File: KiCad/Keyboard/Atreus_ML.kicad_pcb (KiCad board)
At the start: 2 copper layers, 86 parts, among them K1 CHERRY_ML, K10 CHERRY_ML, K11 CHERRY_ML, K12 CHERRY_ML, K13 CHERRY_ML, K14 CHERRY_ML, K15 CHERRY_ML, K16 CHERRY_ML, K17 CHERRY_ML, K18 CHERRY_ML, K19 CHERRY_ML, K2 CHERRY_ML, K20 CHERRY_ML, K21 CHERRY_ML, K22 CHERRY_ML, K23 CHERRY_ML, K24 CHERRY_ML, K25 CHERRY_ML, K26 CHERRY_ML, K27 CHERRY_ML, K28 CHERRY_ML, K29 CHERRY_ML, K3 CHERRY_ML, K30 CHERRY_ML, K31 CHERRY_ML, K32 CHERRY_ML, K33 CHERRY_ML, K34 CHERRY_ML, K35 CHERRY_ML, K36 CHERRY_ML, K37 CHERRY_ML, K38 CHERRY_ML, K39 CHERRY_ML, K4 CHERRY_ML, K40 CHERRY_ML, K41 CHERRY_ML, K42 CHERRY_ML, K5 CHERRY_ML, K6 CHERRY_ML, K7 CHERRY_ML, K8 CHERRY_ML, K9 CHERRY_ML, P1 CONN_01X07, U1 TEENSY2.0

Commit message: Switching to teensu compact
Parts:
- moved P1 67.9 mm to (158.0, 104.0), turned to 180 degrees
- moved U1 45.8 mm to (150.0, 80.0)
- moved K2 26.5 mm to (51.0, 86.0)
- moved D2 26.3 mm to (50.0, 97.0)
- moved D6 25.1 mm to (70.0, 96.0)
- moved K6 23.9 mm to (71.0, 86.0)
- moved D1 23.0 mm to (50.0, 76.0)
- moved D5 22.6 mm to (70.0, 73.0)
- moved K1 22.1 mm to (50.0, 67.0)
- moved D10 22.1 mm to (90.0, 91.0)
- moved K5 21.0 mm to (70.0, 64.0)
- moved K10 19.7 mm to (91.0, 81.0)
- moved D9 19.2 mm to (90.0, 68.0)
- moved K9 16.8 mm to (90.0, 59.0)
- moved K35 16.6 mm to (261.0, 56.0)
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
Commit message: Basic Layout done
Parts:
- removed P1: CONN_01X07, Socket_Strips:Socket_Strip_Straight_1x07
- U1: value TEENSY2.0 -> TEENSY2.0-Compact; footprint Teensy:TEENSY_2.0 -> Teensy:TEENSY_2.0-Compact
- moved D12 44.3 mm to (90.0, 128.0)
- moved D4 42.6 mm to (50.0, 136.0)
- moved D8 41.5 mm to (70.0, 133.0)
- moved U1 41.4 mm to (156.0, 39.0)
- moved K4 39.9 mm to (50.0, 127.0)
- moved D3 39.8 mm to (50.0, 116.0)
- moved D7 38.8 mm to (70.0, 113.0)
- moved K12 38.5 mm to (90.0, 119.0)
- moved K8 38.3 mm to (70.0, 124.0)
- moved K3 35.4 mm to (50.0, 107.0)
- moved D16 34.8 mm to (110.0, 134.0)
- moved K7 33.7 mm to (70.0, 104.0)
- moved D11 32.9 mm to (90.0, 108.0)
- moved K11 30.7 mm to (90.0, 99.0)
- moved D34 29.6 mm to (230.0, 128.0), turned to 0 degrees
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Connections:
- U1 pad 19: Net-(K21-Pad4) -> Net-(U1-Pad19)

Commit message: Rotation done
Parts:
- moved D20 25.2 mm to (105.3, 145.3), turned to 350 degrees
- moved D21 24.9 mm to (126.8, 138.9), turned to 170 degrees
- moved D4 24.3 mm to (27.2, 127.5), turned to 350 degrees
- moved K20 23.6 mm to (107.1, 135.5), turned to 350 degrees
- moved D16 23.4 mm to (86.7, 135.9), turned to 350 degrees
- moved K21 23.3 mm to (128.5, 129.1), turned to 350 degrees
- moved D8 23.1 mm to (47.5, 128.0), turned to 350 degrees
- moved K4 22.8 mm to (28.8, 118.6), turned to 350 degrees
- moved D12 22.0 mm to (68.0, 126.6), turned to 350 degrees
- moved K16 21.9 mm to (88.2, 127.1), turned to 350 degrees
- moved D19 21.8 mm to (109.0, 124.6), turned to 350 degrees
- moved K8 21.5 mm to (49.0, 119.1), turned to 350 degrees
- moved D3 21.0 mm to (30.7, 107.8), turned to 350 degrees
- moved K12 20.5 mm to (69.6, 117.7), turned to 350 degrees
- moved K19 20.3 mm to (110.5, 115.8), turned to 350 degrees
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
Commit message: Layout done!
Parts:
- moved U1 69.5 mm to (150.0, 98.0)
- moved D23 9.55 mm to (177.1, 85.2)
- moved D25 9.55 mm to (184.0, 124.6)
- moved D26 9.55 mm to (187.5, 144.3)
- moved D28 9.55 mm to (199.5, 97.5)
- moved D29 9.55 mm to (202.8, 116.2)
- moved D30 9.55 mm to (206.3, 135.9)
- moved D31 9.55 mm to (214.5, 67.5)
- moved D32 9.55 mm to (218.2, 88.1)
- moved D33 9.55 mm to (221.5, 106.9)
- moved D34 9.55 mm to (225.0, 126.6)
- moved D39 9.55 mm to (255.3, 68.4)
- moved D40 9.55 mm to (259.0, 89.1)
- moved D41 9.55 mm to (262.4, 108.8)
- moved K24 9.55 mm to (179.0, 96.1)
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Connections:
- K22 pad 3: Net-(K22-Pad3) -> Net-(K21-Pad4)
- K22 pad 4: Net-(K21-Pad4) -> Net-(K22-Pad4)
- U1 pad 19: Net-(U1-Pad19) -> Net-(K21-Pad4)

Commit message: Rev one is done!
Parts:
- moved D36 1.62 mm to (239.0, 88.0), turned to 190 degrees
- moved D37 1.31 mm to (242.0, 108.0), turned to 190 degrees
- moved D32 1.16 mm to (218.0, 87.0), turned to 190 degrees
- moved D40 1.08 mm to (259.0, 88.0), turned to 190 degrees
- moved D39 0.90 mm to (256.0, 69.0), turned to 190 degrees
- moved D41 0.89 mm to (262.0, 108.0), turned to 190 degrees
- moved D26 0.85 mm to (188.0, 145.0), turned to 190 degrees
- moved D28 0.66 mm to (200.0, 98.0), turned to 190 degrees
- moved D31 0.65 mm to (215.0, 67.0), turned to 190 degrees
- moved D25 0.64 mm to (184.0, 124.0), turned to 190 degrees
- moved D42 0.55 mm to (266.0, 127.0), turned to 190 degrees
- moved D38 0.52 mm to (245.0, 128.0), turned to 190 degrees
- moved D33 0.51 mm to (221.0, 107.0), turned to 190 degrees
- moved D24 0.47 mm to (181.0, 105.0), turned to 190 degrees
- moved D34 0.45 mm to (225.0, 127.0), turned to 190 degrees
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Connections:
- U1 pad 2: Net-(D1-Pad2) -> Net-(D17-Pad2)
- U1 pad 25: Net-(D27-Pad2) -> Net-(D39-Pad2)
- U1 pad 26: Net-(D31-Pad2) -> Net-(D35-Pad2)
- U1 pad 27: Net-(D35-Pad2) -> Net-(D31-Pad2)
- U1 pad 28: Net-(D39-Pad2) -> Net-(D27-Pad2)
- U1 pad 3: Net-(D5-Pad2) -> Net-(D13-Pad2)
- U1 pad 5: Net-(D13-Pad2) -> Net-(D5-Pad2)
- U1 pad 6: Net-(D17-Pad2) -> Net-(D1-Pad2)
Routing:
- net Net-(D1-Pad2): track 0.00 -> 214.9 mm
- net Net-(D5-Pad2): track 0.00 -> 186.8 mm
- net Net-(D10-Pad2): track 0.00 -> 157.9 mm
- net Net-(D13-Pad2): track 0.00 -> 130.4 mm
- net Net-(K20-Pad4): track 0.00 -> 101.1 mm
- net Net-(D22-Pad2): track 0.00 -> 98.7 mm
- net Net-(D17-Pad2): track 0.00 -> 94.5 mm
- net Net-(D31-Pad2): track 0.00 -> 76.2 mm
- net Net-(D35-Pad2): track 0.00 -> 75.9 mm
- net Net-(D27-Pad2): track 0.00 -> 75.7 mm
- net Net-(D39-Pad2): track 0.00 -> 74.9 mm
- net Net-(K18-Pad4): track 0.00 -> 71.1 mm
- net Net-(K19-Pad4): track 0.00 -> 64.0 mm
- net Net-(K21-Pad4): track 0.00 -> 37.1 mm
- net Net-(K4-Pad4): track 0.00 -> 17.4 mm
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
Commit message: Last cleanup
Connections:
- U1 pad 25: Net-(D39-Pad2) -> Net-(D27-Pad2)
- U1 pad 26: Net-(D35-Pad2) -> Net-(D31-Pad2)
- U1 pad 27: Net-(D31-Pad2) -> Net-(D35-Pad2)
- U1 pad 28: Net-(D27-Pad2) -> Net-(D39-Pad2)
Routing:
- net Net-(D39-Pad2): track 74.9 -> 196.3 mm
- net Net-(D35-Pad2): track 75.9 -> 175.8 mm
- net Net-(D31-Pad2): track 76.2 -> 154.9 mm
- net Net-(K17-Pad4): track 0.00 -> 70.1 mm, vias 0 -> 2
- net Net-(D27-Pad2): track 75.7 -> 136.6 mm

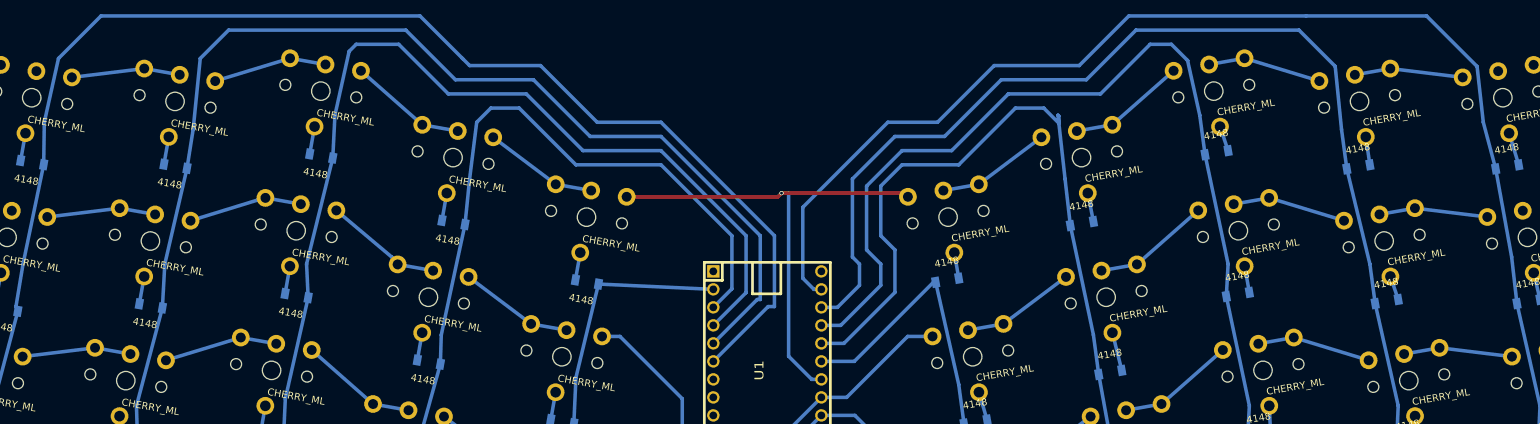
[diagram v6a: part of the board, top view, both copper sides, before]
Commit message: Starting rev 2, cleaning up columns
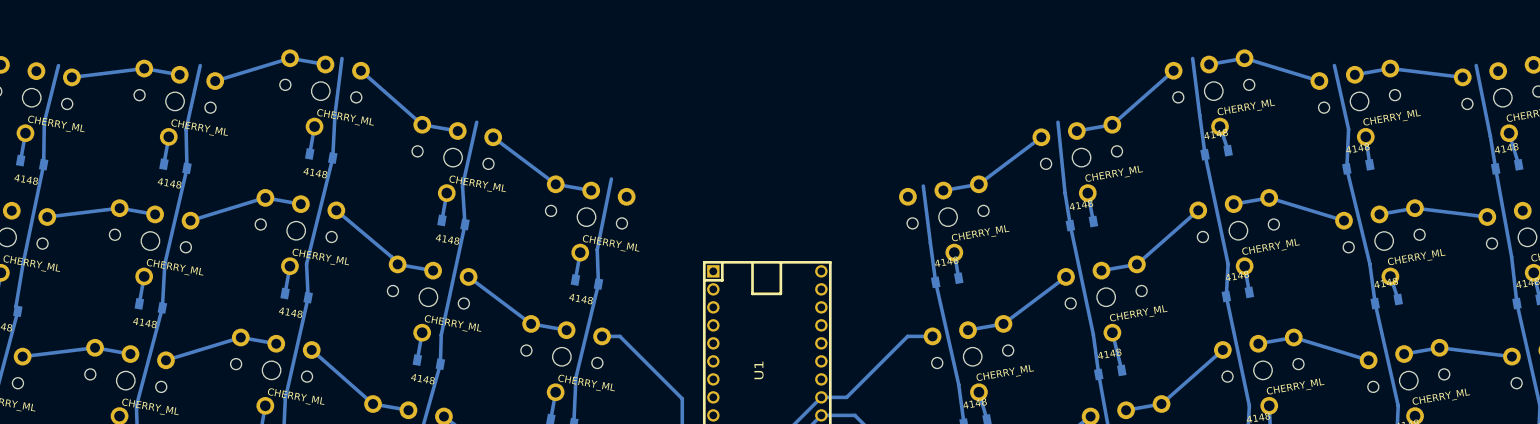
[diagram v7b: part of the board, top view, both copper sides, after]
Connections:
- U1 pad 25: Net-(D27-Pad2) -> Net-(D39-Pad2)
- U1 pad 26: Net-(D31-Pad2) -> Net-(D35-Pad2)
- U1 pad 27: Net-(D35-Pad2) -> Net-(D31-Pad2)
- U1 pad 28: Net-(D39-Pad2) -> Net-(D27-Pad2)
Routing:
- net Net-(D1-Pad2): track 214.9 -> 75.8 mm
- net Net-(D39-Pad2): track 196.3 -> 73.9 mm
- net Net-(D5-Pad2): track 186.8 -> 75.0 mm
- net Net-(D35-Pad2): track 175.8 -> 75.0 mm
- net Net-(D10-Pad2): track 157.9 -> 74.5 mm
- net Net-(D31-Pad2): track 154.9 -> 75.0 mm
- net Net-(K17-Pad4): track 70.1 -> 0.72 mm, vias 2 -> 1
- net Net-(D27-Pad2): track 136.6 -> 74.7 mm
- net Net-(D13-Pad2): track 130.4 -> 75.1 mm
- net Net-(D22-Pad2): track 98.7 -> 92.0 mm
- net Net-(D17-Pad2): track 94.5 -> 93.3 mm

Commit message: Rev 2 is done
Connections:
- U1 pad 24: Net-(D22-Pad2) -> Net-(D39-Pad2)
- U1 pad 25: Net-(D39-Pad2) -> Net-(D35-Pad2)
- U1 pad 26: Net-(D35-Pad2) -> Net-(D31-Pad2)
- U1 pad 27: Net-(D31-Pad2) -> Net-(D27-Pad2)
- U1 pad 28: Net-(D27-Pad2) -> Net-(D22-Pad2)
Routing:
- net Net-(D39-Pad2): track 73.9 -> 206.4 mm
- net Net-(D1-Pad2): track 75.8 -> 208.3 mm
- net Net-(D5-Pad2): track 75.0 -> 182.9 mm
- net Net-(K17-Pad4): track 0.72 -> 108.3 mm
- net Net-(D35-Pad2): track 75.0 -> 182.4 mm
- net Net-(D10-Pad2): track 74.5 -> 155.9 mm
- net Net-(D31-Pad2): track 75.0 -> 156.4 mm
- net Net-(D13-Pad2): track 75.1 -> 130.4 mm
- net Net-(D27-Pad2): track 74.7 -> 129.1 mm
- net Net-(D22-Pad2): track 92.0 -> 118.8 mm
- net Net-(D17-Pad2): track 93.3 -> 119.3 mm
- net Net-(K18-Pad4): track 71.1 -> 83.7 mm
- net Net-(K19-Pad4): track 64.0 -> 70.4 mm
